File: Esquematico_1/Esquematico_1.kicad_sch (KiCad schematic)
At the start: 0 parts

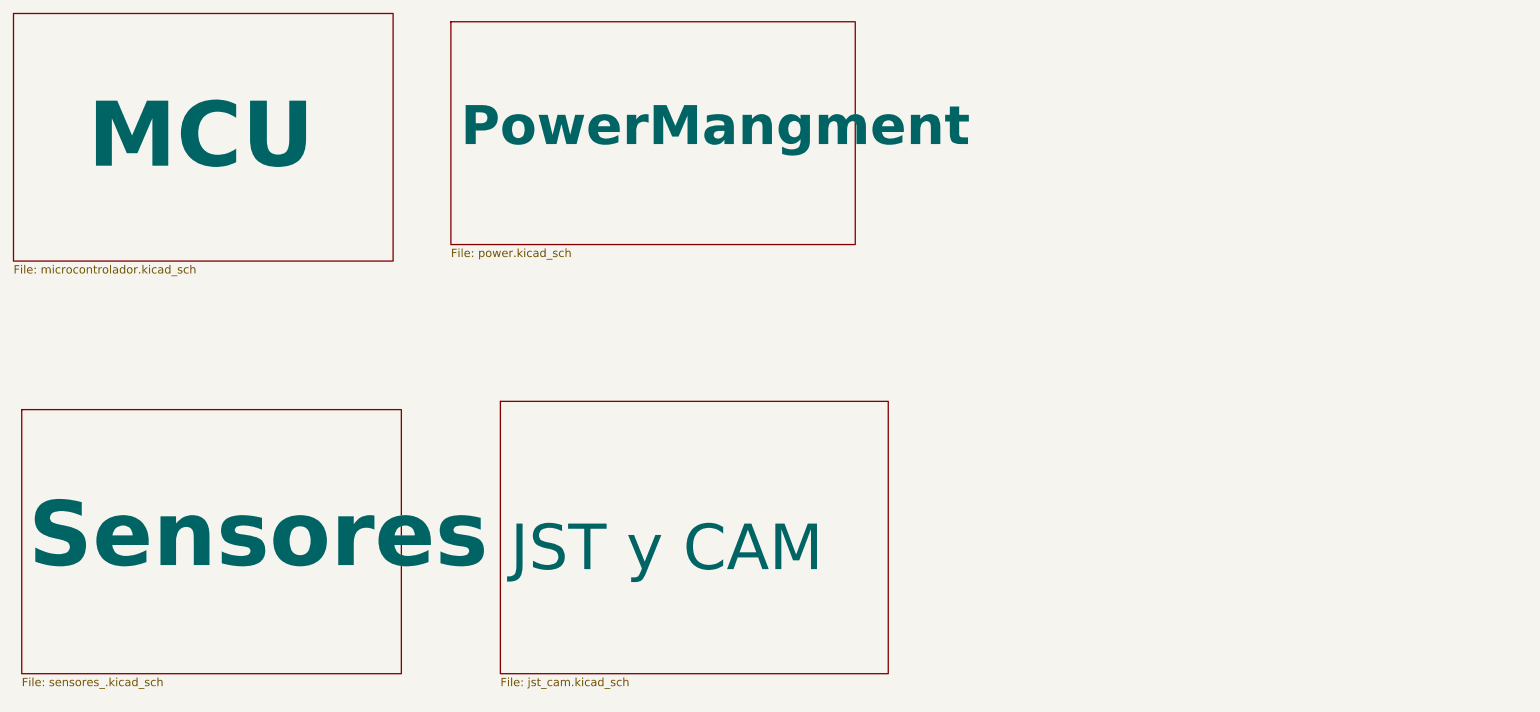
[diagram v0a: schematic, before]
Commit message: Update footprint library
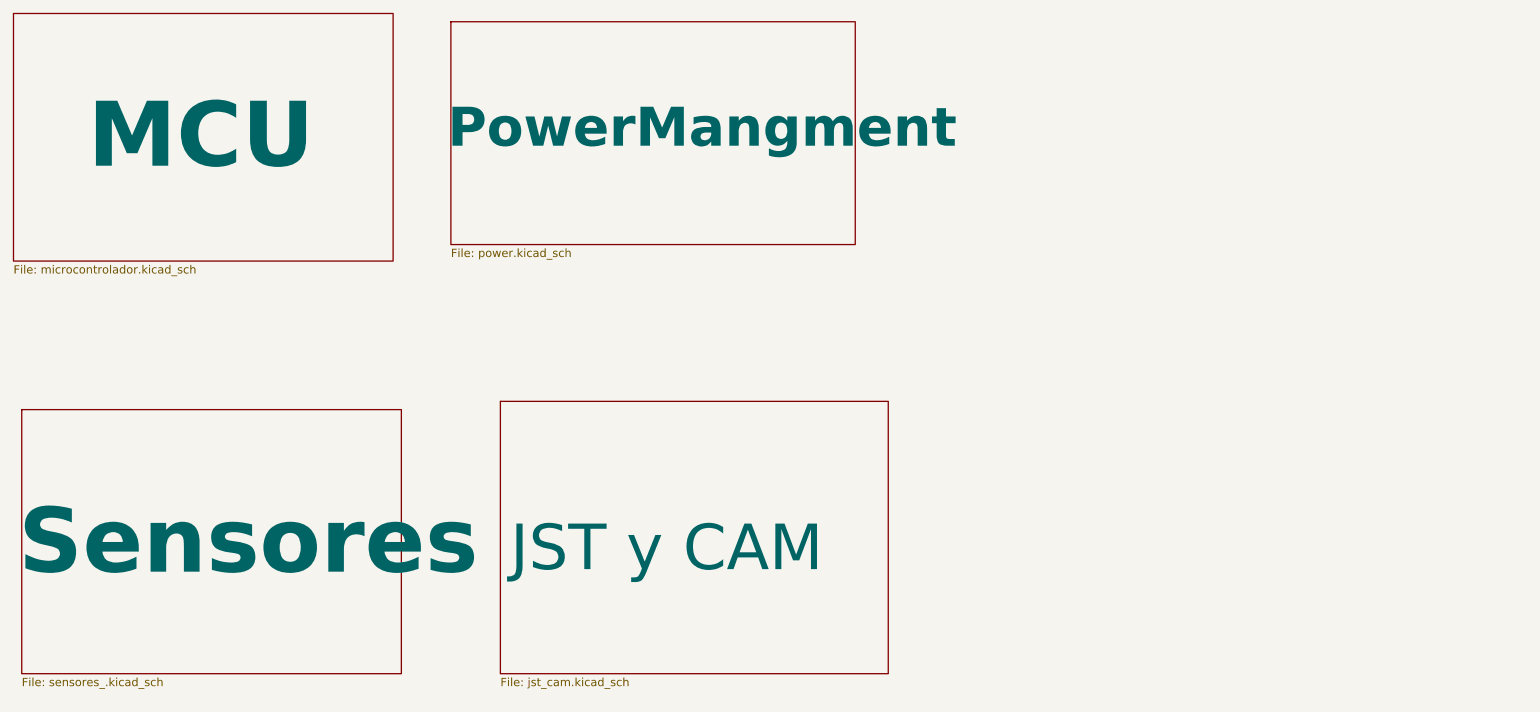
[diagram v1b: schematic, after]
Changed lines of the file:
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@@
 		)
 		(property "Sheetname" "PowerMangment"
-			(at 96.774 46.228 0)
+			(at 94.742 46.482 0)
 			(effects
 				(font
@@
 		)
 		(property "Sheetname" "Sensores"
-			(at 30.226 111.506 0)
+			(at 28.702 112.522 0)
 			(effects
 				(font

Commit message: Update
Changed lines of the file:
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@@
 	)
 	(sheet
-		(at 95.25 26.67)
+		(at 101.6 26.67)
 		(size 62.23 34.29)
 		(exclude_from_sim no)
@@
 		)
 		(property "Sheetname" "PowerMangment"
-			(at 94.742 46.482 0)
+			(at 101.092 46.482 0)
 			(effects
 				(font
@@
 		)
 		(property "Sheetfile" "power.kicad_sch"
-			(at 95.25 61.5446 0)
+			(at 101.6 61.5446 0)
 			(effects
 				(font
@@
 		)
 		(property "Sheetname" "Sensores"
-			(at 28.702 112.522 0)
+			(at 28.956 112.014 0)
 			(effects
 				(font

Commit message: Update llamada
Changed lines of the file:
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@@
 		)
 		(property "Sheetname" "PowerMangment"
-			(at 101.092 46.482 0)
+			(at 102.108 44.45 0)
 			(effects
 				(font
@@
 		)
 		(property "Sheetname" "Sensores"
-			(at 28.956 112.014 0)
+			(at 30.988 110.49 0)
 			(effects
 				(font
@@
 		)
 		(property "Sheetname" "MCU"
-			(at 39.37 44.196 0)
+			(at 35.814 39.624 0)
 			(effects
 				(font

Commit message: Update footprint sw rst
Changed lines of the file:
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@@
 		)
 		(property "Sheetname" "PowerMangment"
-			(at 102.108 44.45 0)
+			(at 102.87 45.466 0)
 			(effects
 				(font
@@
 		)
 		(property "Sheetname" "Sensores"
-			(at 30.988 110.49 0)
+			(at 30.734 109.982 0)
 			(effects
 				(font
@@
 		)
 		(property "Sheetname" "MCU"
-			(at 35.814 39.624 0)
+			(at 39.878 44.45 0)
 			(effects
 				(font

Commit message: Todos los footprints menos ESC
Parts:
- added H1, H2, H3, H4: MountingHole, MountingHole:MountingHole_2.7mm_M2.5_Pad_Via, symbol Mechanical:MountingHole

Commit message: BIG Update conexionado MCU y PCB
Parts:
- H1, H2, H3, H4: footprint MountingHole:MountingHole_2.7mm_M2.5_Pad_Via -> MountingHole:MountingHole_3.2mm_M3_Pad_Via
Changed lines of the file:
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@@
 			)
 		)
-		(property "Footprint" "MountingHole:MountingHole_2.7mm_M2.5_Pad_Via"
+		(property "Footprint" "MountingHole:MountingHole_3.2mm_M3_Pad_Via"
 			(at 242.57 76.2 0)
 			(effects
@@
 			)
 		)
-		(property "Footprint" "MountingHole:MountingHole_2.7mm_M2.5_Pad_Via"
+		(property "Footprint" "MountingHole:MountingHole_3.2mm_M3_Pad_Via"
 			(at 219.71 88.9 0)
 			(effects
@@
 			)
 		)
-		(property "Footprint" "MountingHole:MountingHole_2.7mm_M2.5_Pad_Via"
+		(property "Footprint" "MountingHole:MountingHole_3.2mm_M3_Pad_Via"
 			(at 219.71 76.2 0)
 			(effects
@@
 			)
 		)
-		(property "Footprint" "MountingHole:MountingHole_2.7mm_M2.5_Pad_Via"
+		(property "Footprint" "MountingHole:MountingHole_3.2mm_M3_Pad_Via"
 			(at 242.57 88.9 0)
 			(effects

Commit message: Cambios de Diodos
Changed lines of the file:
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@@
 	)
 	(sheet
-		(at 102.87 85.09)
-		(size 59.69 41.91)
+		(at 102.87 86.36)
+		(size 59.69 40.64)
 		(exclude_from_sim no)
 		(in_bom yes)
@@
 		)
 		(property "Sheetname" "JST y CAM"
-			(at 104.394 111.76 0)
+			(at 104.394 113.03 0)
 			(effects
 				(font
@@
 		)
 		(property "Sheetfile" "jst_cam.kicad_sch"
-			(at 102.87 127.5846 0)
+			(at 102.87 128.8546 0)
 			(effects
 				(font
@@
 	)
 	(sheet
-		(at 101.6 26.67)
-		(size 62.23 34.29)
+		(at 101.6 25.4)
+		(size 62.23 38.1)
 		(exclude_from_sim no)
 		(in_bom yes)
@@
 		)
 		(property "Sheetname" "PowerMangment"
-			(at 102.87 45.466 0)
+			(at 102.87 44.196 0)
 			(effects
 				(font
@@
 		)
 		(property "Sheetfile" "power.kicad_sch"
-			(at 101.6 61.5446 0)
+			(at 101.6 60.2746 0)
 			(effects
 				(font
